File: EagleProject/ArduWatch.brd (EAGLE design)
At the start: 35.5 x 42.9 mm, 23 parts, among them IC1 DS1307Z, IC2 MCP73831, J1 FTS-105-01-L-D, Q1 32.768Hz, U1 ATMEGA328P_TQFP

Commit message: PCB release
PCB release
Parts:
- added DRILEGEND: (no value), drilegend:DRILEGEND
- H5: value MOUNT-HOLE4.1 -> MOUNT-HOLE3.0; device holes:4,1 -> holes:3,0
- USB+, USB-: value WIREPAD2,54/0,8 -> WIREPAD3,81/1,1; device wirepad:2,54/0,8 -> wirepad:3,81/1,1
- moved H5 7.71 mm to (3.68, 40.6)
- moved USB+ 7.25 mm to (2.16, 33.3)
- moved Q1 7.00 mm to (16.6, 15.4)
- moved B+ 6.75 mm to (11.9, 37.1)
- moved C1 6.75 mm to (9.53, 33.4)
- moved C5 6.75 mm to (13.7, 33.4)
- moved C2 6.75 mm to (5.71, 29.0)
- moved C3 6.75 mm to (5.71, 26.5)
- moved IC2 6.75 mm to (9.53, 24.9)
- moved J1 6.75 mm to (17.1, 10.9)
- moved LED1 6.75 mm to (8.64, 31.2)
- moved R1 6.75 mm to (12.1, 28.7)
- moved R2 6.75 mm to (12.1, 24.9)
- moved R3 6.75 mm to (23.5, 24.9)
- moved R4 6.75 mm to (23.5, 27.2)
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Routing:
- net D12: track 51.0 -> 159.3 mm, vias 2 -> 0
- net D11: track 63.0 -> 124.8 mm
- net D13: track 48.2 -> 91.6 mm
- net GND: track 68.4 -> 64.2 mm
- net VUSB: track 12.2 -> 14.8 mm
- net RESET: track 40.0 -> 38.7 mm
- net VCC: track 88.1 -> 89.2 mm
- net N$2: track 6.92 -> 6.16 mm
- net N$5: track 9.99 -> 9.23 mm
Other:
- board size 35.5 x 42.9 mm -> 41.3 x 56.2 mm
- board text added: "ArduWatch"
- board text added: "USB Charger"

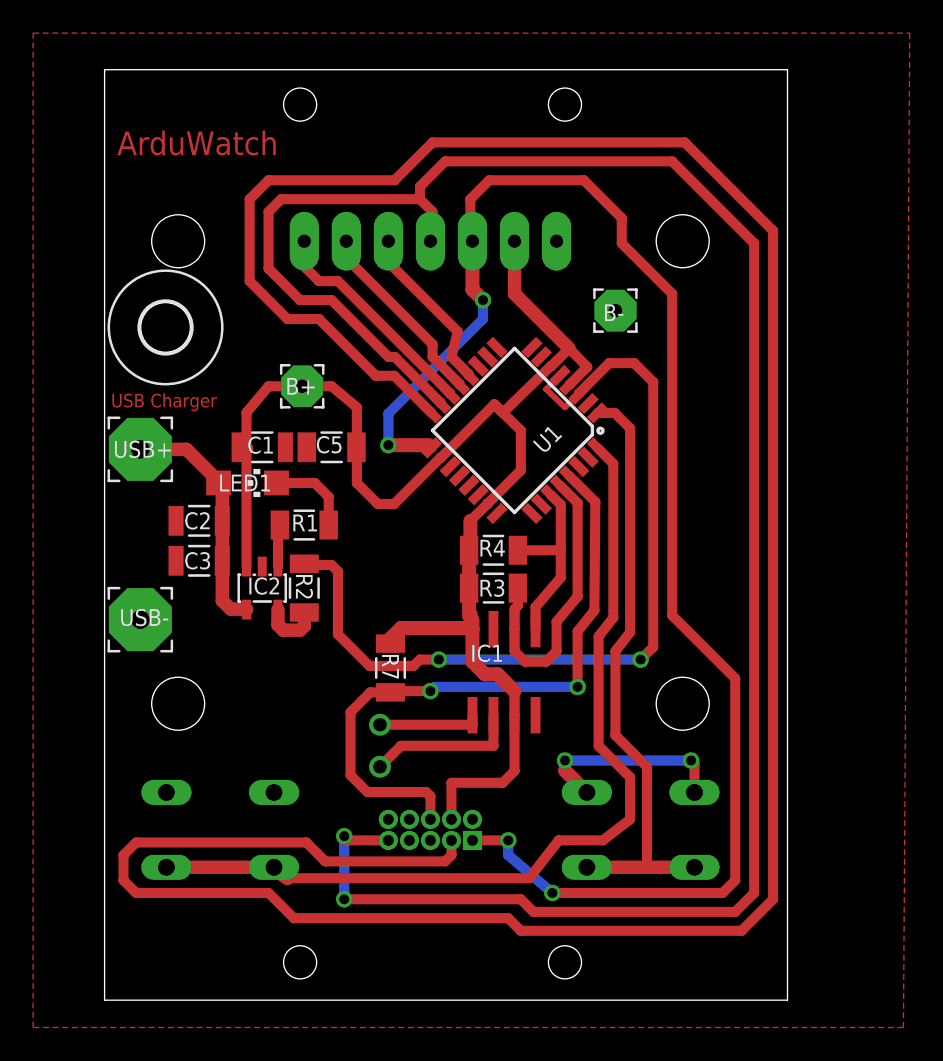
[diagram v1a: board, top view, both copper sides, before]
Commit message: PCB - SPI as Arduino
Change connector for SPI Target
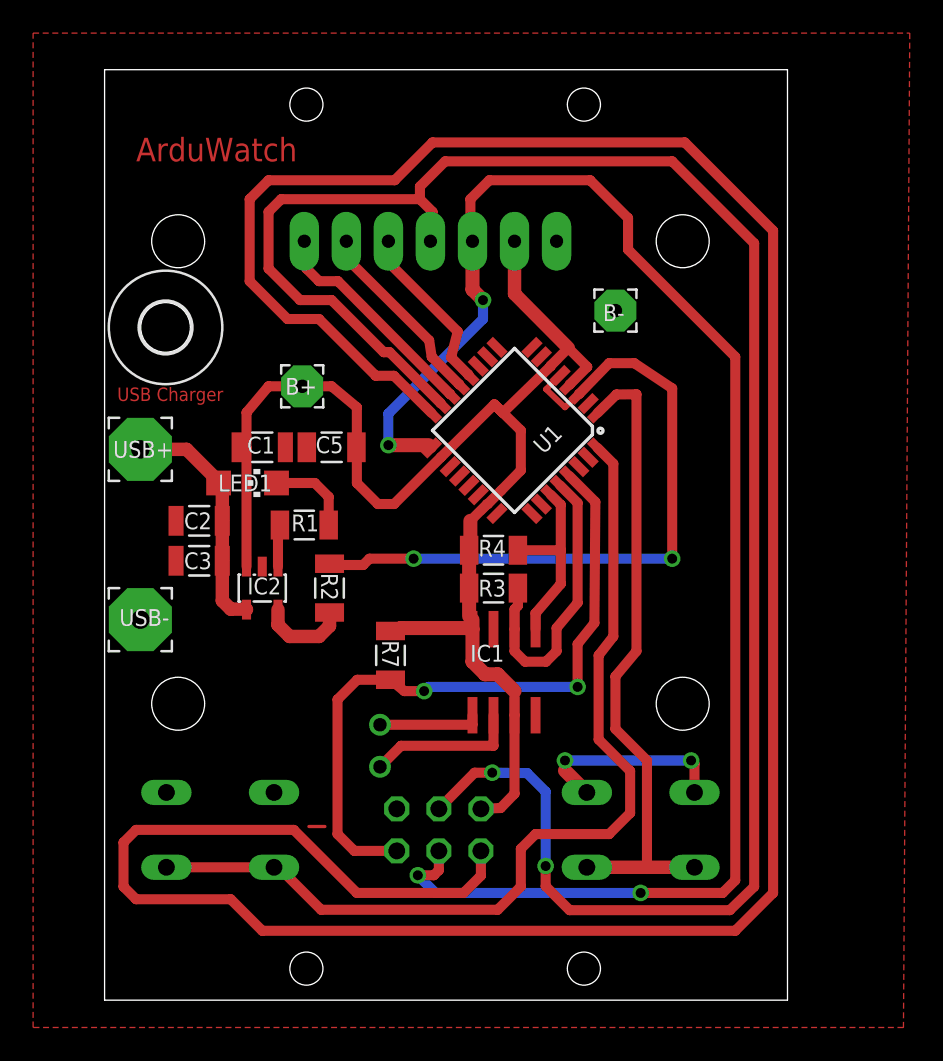
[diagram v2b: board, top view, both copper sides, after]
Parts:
- removed J1: FTS-105-01-L-D, SAMTEC-HTSW-FTxx_By_element14_Batch_1:SAMTEC_FTS-105-01-L-D
- added JP1: (no value), pinhead:2X03
- moved DRILEGEND 15.1 mm to (51.9, 38.2)
- moved R2 1.52 mm to (13.6, 24.9)
- moved R7 0.76 mm to (17.3, 20.8)
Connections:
- net D11: now also JP1.4; no longer J1.9
- net D12: now also JP1.1; no longer J1.3
- net D13: now also JP1.3; no longer J1.1
- net GND: now also JP1.6; no longer J1.2
- net RESET: now also JP1.5; no longer J1.6
- net VCC: now also JP1.2; no longer J1.4
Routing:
- net GND: track 64.2 -> 54.1 mm
- net D11: track 124.8 -> 119.4 mm
- net D13: track 91.6 -> 96.3 mm
- net D12: track 159.3 -> 163.9 mm
- net VCC: track 89.2 -> 86.1 mm
- net BUTTON2: track 36.5 -> 39.1 mm
- net BUTTON1: track 53.8 -> 56.4 mm
- net RESET: track 38.7 -> 41.2 mm
- net N$4: track 3.56 -> 5.40 mm
- net N$7: track 0.00 -> 0.97 mm

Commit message: USB port for charging
Implement USB port for chrging
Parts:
- removed USB+, USB-: WIREPAD3,81/1,1, wirepad:3,81/1,1
- added J1: USB-MICROB, SparkFun-Connectors:USB-MICROB
- moved DRILEGEND 6.87 mm to (52.2, 45.0)
- moved C2 3.81 mm to (5.71, 25.1)
- moved C3 3.43 mm to (5.71, 23.1)
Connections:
- net GND: now also J1.GND, J1.MT1, J1.MT2; no longer USB-.1
- net VUSB: now also J1.VBUS; no longer USB+.1
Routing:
- net GND: track 54.1 -> 63.5 mm
- net VUSB: track 14.8 -> 16.5 mm
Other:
- board text removed: "USB Charger"

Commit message: Add CRYSTAL
Add CRYSTAL 8MHz
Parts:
- added Q2: 8MHz, crystal:HC49/S
- moved B- 22.6 mm to (8.38, 39.4)
- moved H5 1.37 mm to (2.54, 41.4)
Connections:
- new net N$8: Q2.2, U1.7
- new net N$9: Q2.1, U1.8
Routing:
- net GND: track 63.5 -> 92.4 mm
- net N$9: track 0.00 -> 25.0 mm
- net N$8: track 0.00 -> 22.0 mm
- net VCC: track 86.1 -> 84.2 mm
- net N$7: track 0.97 -> 0.38 mm
